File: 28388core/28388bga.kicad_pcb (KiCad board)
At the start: 4 copper layers, 277 parts, among them IC1 F28388DZWTS, IC2 TPS62420DRCT, IC6 OPA4350EA_250, IC7 TPS3702CX33DDCT, IC8 CDCLVC1104PW, IC9 TPS3702CX12DDCT, J9 Conn_02x07_Odd_Even, Q1 FMMT618TA, Q11 AT24C16C-SSHM-T, Q13 DP83822IRHBR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

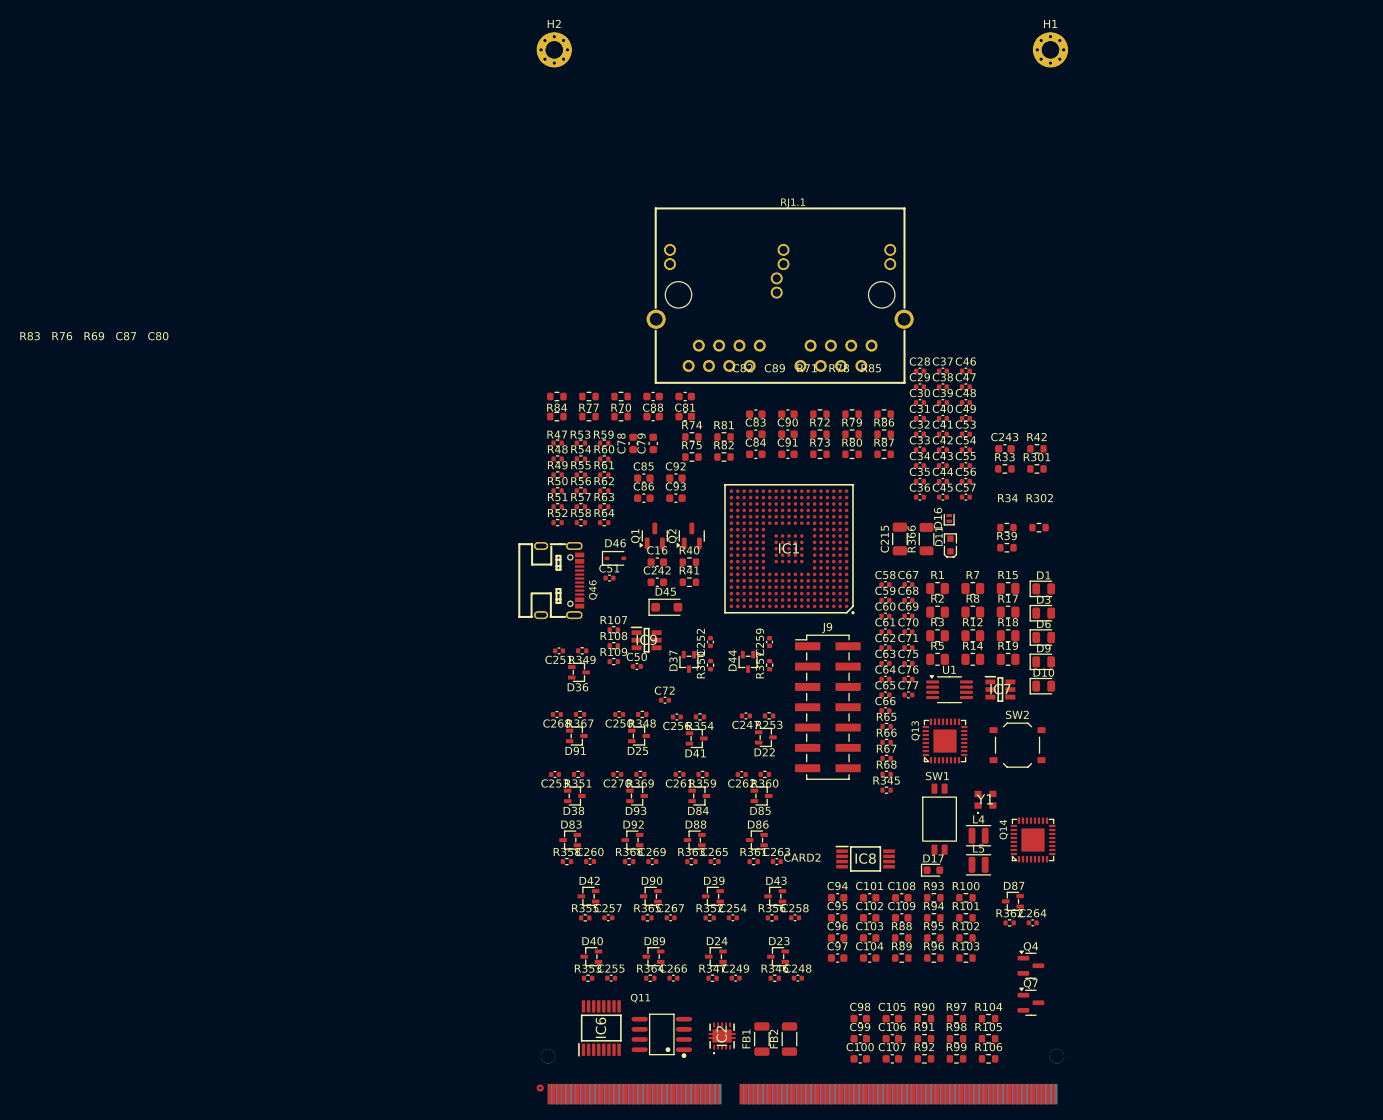
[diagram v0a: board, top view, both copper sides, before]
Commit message: 使用100PIN连接器，试着重新分配引脚
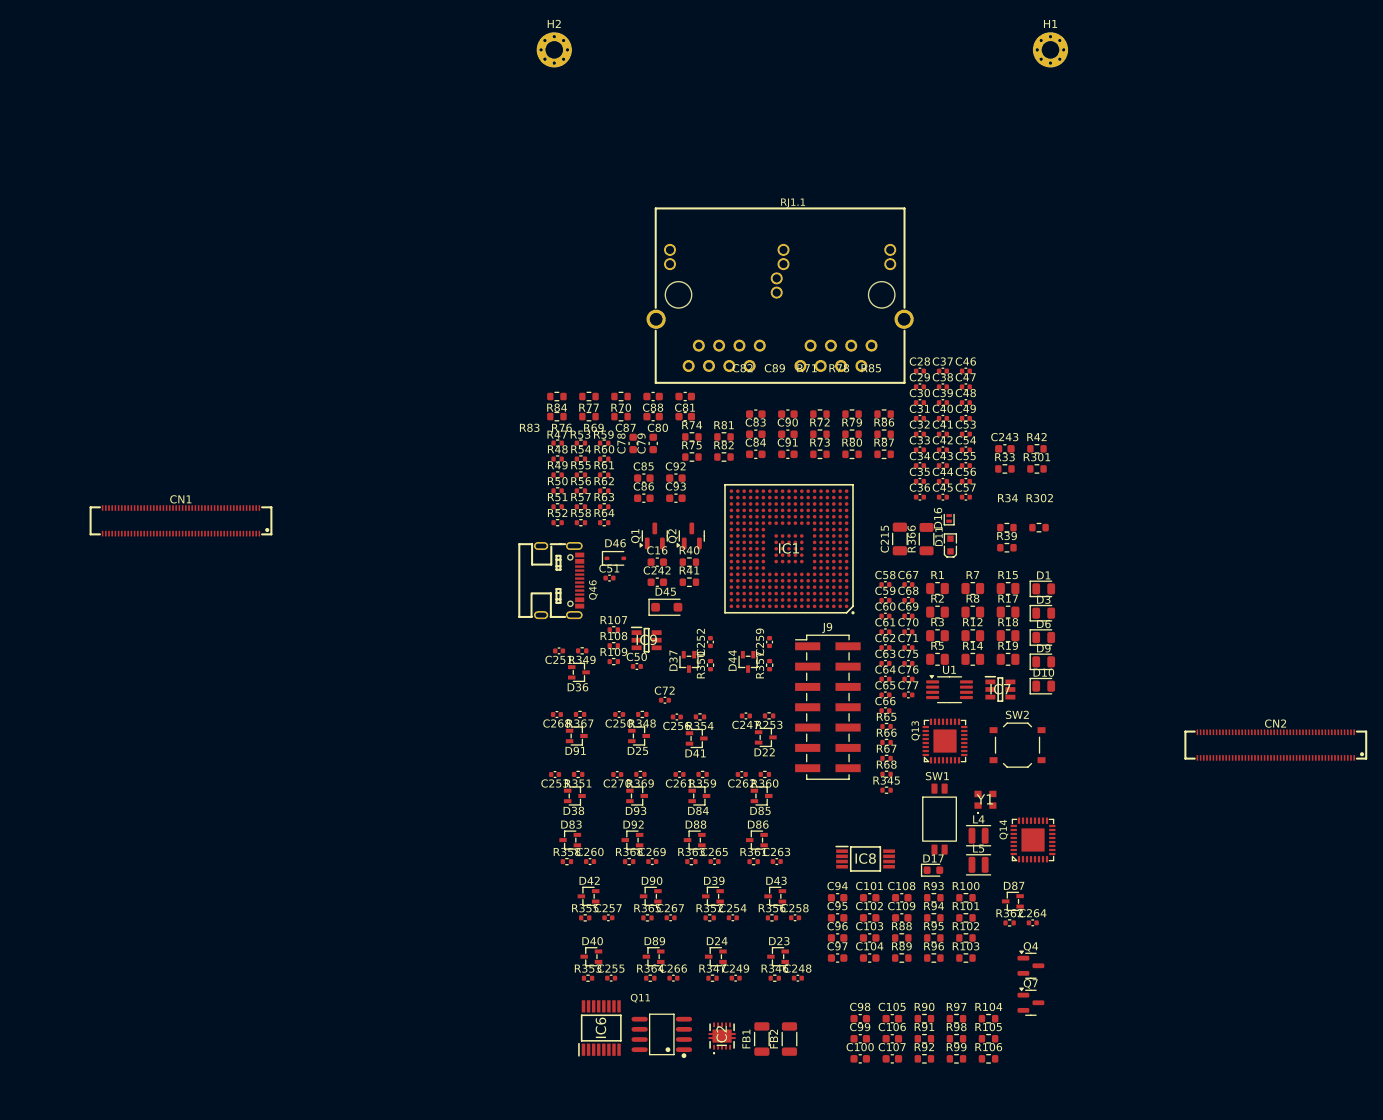
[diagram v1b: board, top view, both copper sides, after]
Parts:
- removed CARD2: DDR3, 1mmlab_footprint:PCBComponent_1 - duplicate
- added CN1: ~, 1mmlab_footprint:CONN-SMD_DF40C-100DS-0.4V-51, F.Cu at (86.7, 86.2)
- added CN2: ~, 1mmlab_footprint:CONN-SMD_DF40C-100DS-0.4V-51, F.Cu at (223.5, 114.2)
